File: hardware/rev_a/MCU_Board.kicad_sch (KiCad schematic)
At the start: 28 parts, among them J1 ST-Link, J2 Conn_01x08, J3 Bus, J4 Conn_01x08, J5 Conn_02x07_Odd_Even, SW1 nRST, U1 STM32F042K6Tx, U3 SN65HVD230, U4 LP2985-3.3, Y1 8Mhz

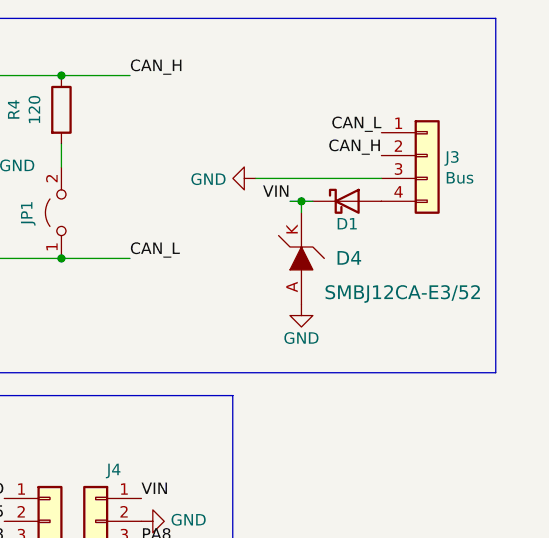
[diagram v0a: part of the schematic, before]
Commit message: Remove the dependancy with external libraries, the TVS diode is now using the default symbol and a custom footprint
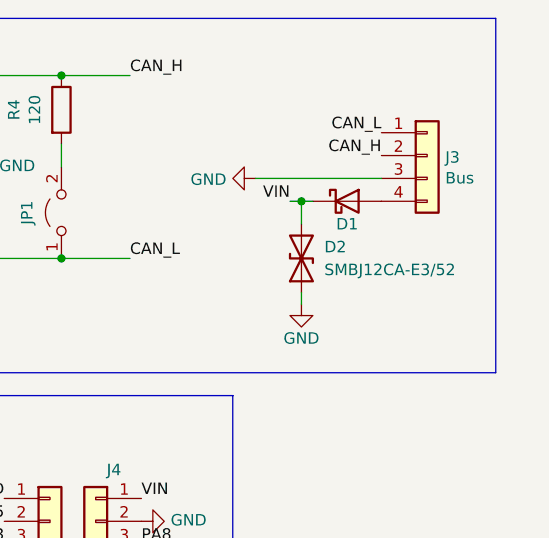
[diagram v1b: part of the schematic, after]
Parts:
- removed D4: SMBJ12CA-E3/52, custom:DO-214AA, symbol dk_TVS-Diodes:ESD5Z3_3T1G
- added D2: SMBJ12CA-E3/52, custom:DO-214AA, symbol Device:D_TVS
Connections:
- net GND: now also D2.1 (A1)
- net VIN: now also D2.2 (A2)
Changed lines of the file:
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@@
+    (stroke (width 0) (type default))
+  )
+  (wire (pts (xy 259.08 54.61) (xy 259.08 55.88))
     (stroke (width 0) (type default))
   )
@@
     (stroke (width 0) (type default))
   )
-  (wire (pts (xy 259.08 44.45) (xy 259.08 45.72))
+  (wire (pts (xy 259.08 44.45) (xy 259.08 46.99))
     (stroke (width 0) (type default))
   )
@@
     )
   )
-  (symbol (lib_id "dk_TVS-Diodes:ESD5Z3_3T1G") (at 259.08 50.8 90) (unit 1)
-    (in_bom yes) (on_board yes) (dnp no)
-    (property "Reference" "D4" (at 262.89 50.8 90)
-      (effects (font (size 1.524 1.524)) (justify right))
-    )
-    (property "Value" "SMBJ12CA-E3/52" (at 261.62 54.61 90)
-      (effects (font (size 1.524 1.524)) (justify right))
-    )
-    (property "Footprint" "custom:DO-214AA" (at 254 45.72 0)
-      (effects (font (size 1.524 1.524)) (justify left) hide)
-    )
-    (property "Datasheet" "https://fr.farnell.com/vishay/smbj12ca-e3-52/diode-tvs-600w-12v-bidir-smb/dp/1698866" (at 251.46 45.72 0)
-      (effects (font (size 1.524 1.524)) (justify left) hide)
-    )
-    (pin "A")
-    (pin "K")
-    (instances
-      (project "MCU_Board"
-        (path "/a4fcdb05-5e54-43b8-a791-cc363feb7f77"
-          (reference "D4") (unit 1)
-        )
-      )
+  (symbol (lib_id "Device:D_TVS") (at 259.08 50.8 90) (unit 1)
+    (in_bom yes) (on_board yes) (dnp no) (fields_autoplaced)
+    (property "Reference" "D2" (at 261.62 49.53 90)
+      (effects (font (size 1.27 1.27)) (justify right))
+    )
+    (property "Value" "SMBJ12CA-E3/52" (at 261.62 52.07 90)
+      (effects (font (size 1.27 1.27)) (justify right))
+    )
+    (property "Footprint" "custom:DO-214AA" (at 259.08 50.8 0)
+      (effects (font (size 1.27 1.27)) hide)
+    )
+    (property "Datasheet" "https://fr.farnell.com/vishay/smbj12ca-e3-52/diode-tvs-600w-12v-bidir-smb/dp/1698866" (at 259.08 50.8 0)
+      (effects (font (size 1.27 1.27)) hide)
+    )
+    (pin "1")
+    (pin "2")
+    (instances
+      (project "MCU_Board"
+        (path "/a4fcdb05-5e54-43b8-a791-cc363feb7f77"
+          (reference "D2") (unit 1)
+        )
+      )

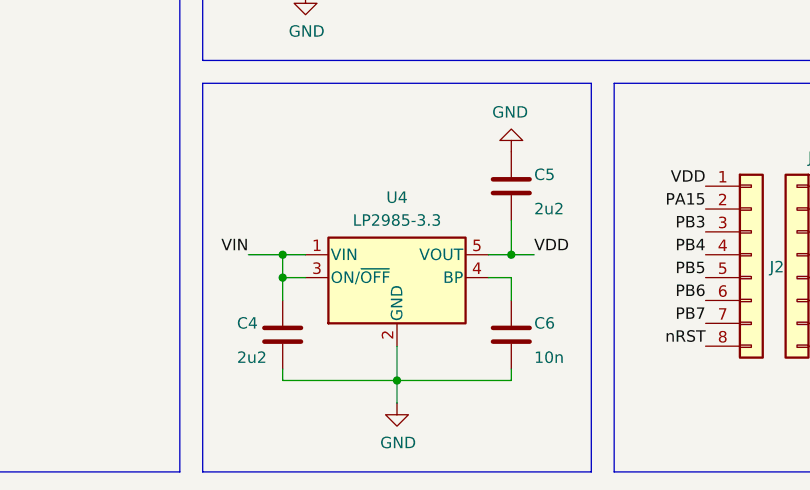
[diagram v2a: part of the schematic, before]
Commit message: Update the reference of various components
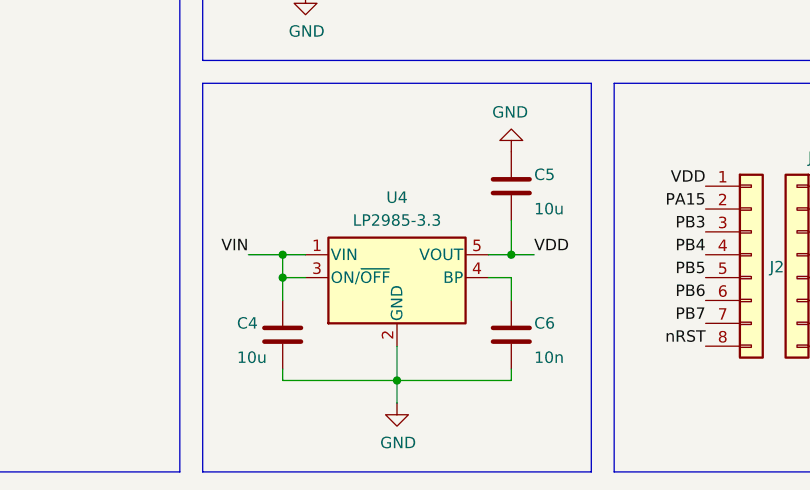
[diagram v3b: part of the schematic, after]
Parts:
- C4, C5: value 2u2 -> 10u
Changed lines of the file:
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@@
       (effects (font (size 1.27 1.27)) (justify left))
     )
-    (property "Value" "2u2" (at 173.99 96.52 0)
+    (property "Value" "10u" (at 173.99 96.52 0)
       (effects (font (size 1.27 1.27)) (justify left))
     )
@@
       (effects (font (size 1.27 1.27)) hide)
     )
-    (property "Datasheet" "https://fr.farnell.com/kemet/c0805c225k4pactu/condensateur-2-2-f-16v-10-x5r/dp/2773238" (at 179.07 93.98 0)
+    (property "Datasheet" "https://fr.farnell.com/walsin/0805x106m250cp/cap-10uf-25v-mlcc-0805/dp/3764157" (at 179.07 93.98 0)
       (effects (font (size 1.27 1.27)) hide)
     )
@@
       (effects (font (size 1.27 1.27)) hide)
     )
-    (property "Datasheet" "~" (at 133.35 74.93 0)
+    (property "Datasheet" "https://fr.farnell.com/amphenol-fci/10129381-914004blf/conn-header-14-voies-2-rangs-2/dp/3881595" (at 133.35 74.93 0)
       (effects (font (size 1.27 1.27)) hide)
     )
@@
       (effects (font (size 1.27 1.27)) (justify left))
     )
-    (property "Value" "2u2" (at 207.01 80.01 0)
+    (property "Value" "10u" (at 207.01 80.01 0)
       (effects (font (size 1.27 1.27)) (justify left))
     )
@@
       (effects (font (size 1.27 1.27)) hide)
     )
-    (property "Datasheet" "https://fr.farnell.com/kemet/c0805c225k4pactu/condensateur-2-2-f-16v-10-x5r/dp/2773238" (at 204.47 77.47 0)
-      (effects (font (size 1.27 1.27)) hide)
-    )
+    (property "Datasheet" "https://fr.farnell.com/walsin/0805x106m250cp/cap-10uf-25v-mlcc-0805/dp/3764157" (at 204.47 77.47 0)
+      (effects (font (size 1.27 1.27)) hide)
+    )

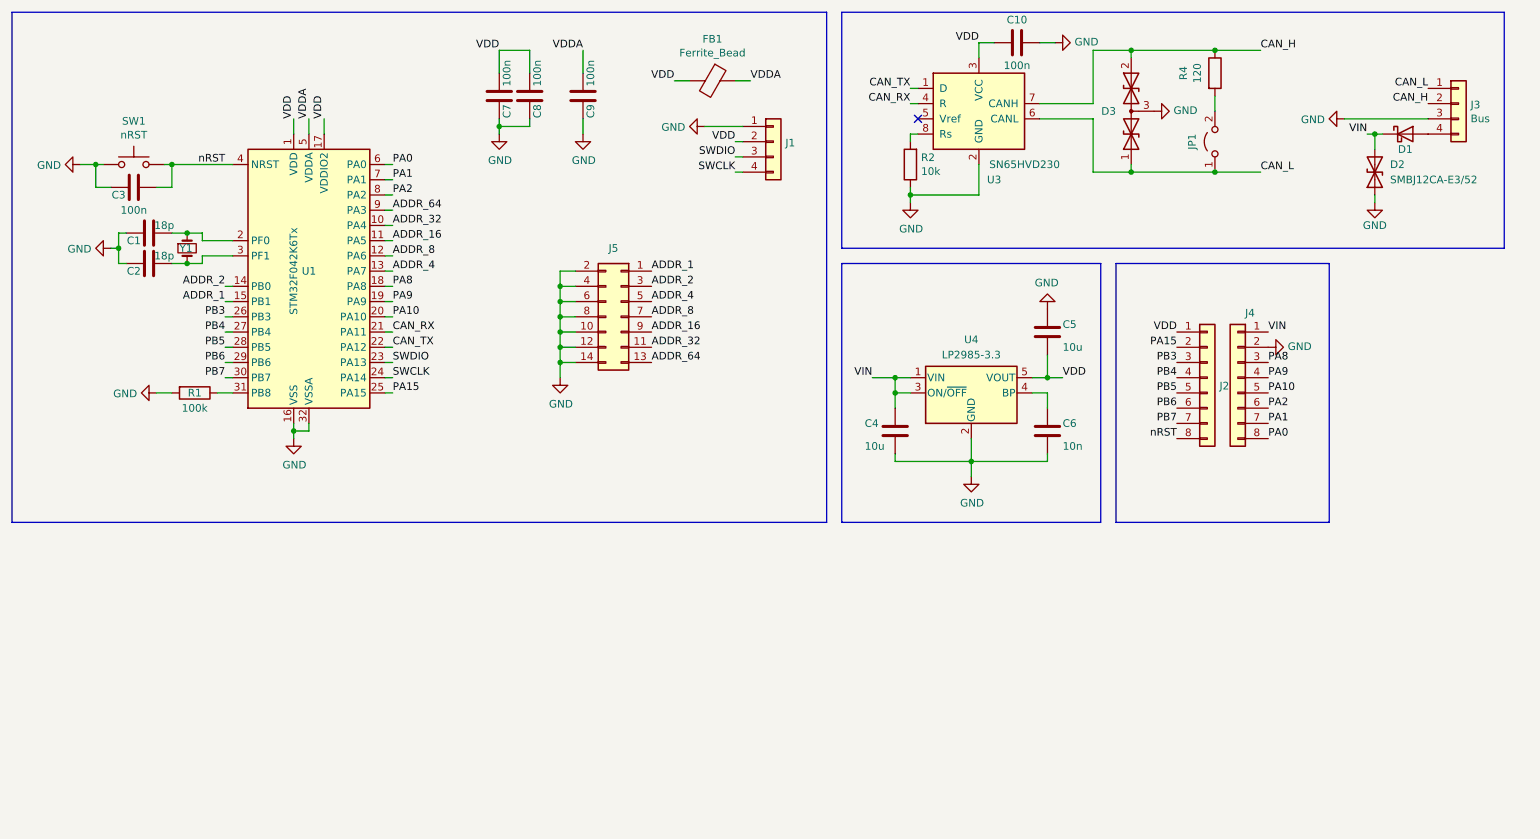
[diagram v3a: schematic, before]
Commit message: Refactorisation de l'étage d'entrée en utilisant un régulateur à découpage DC/DC type buck
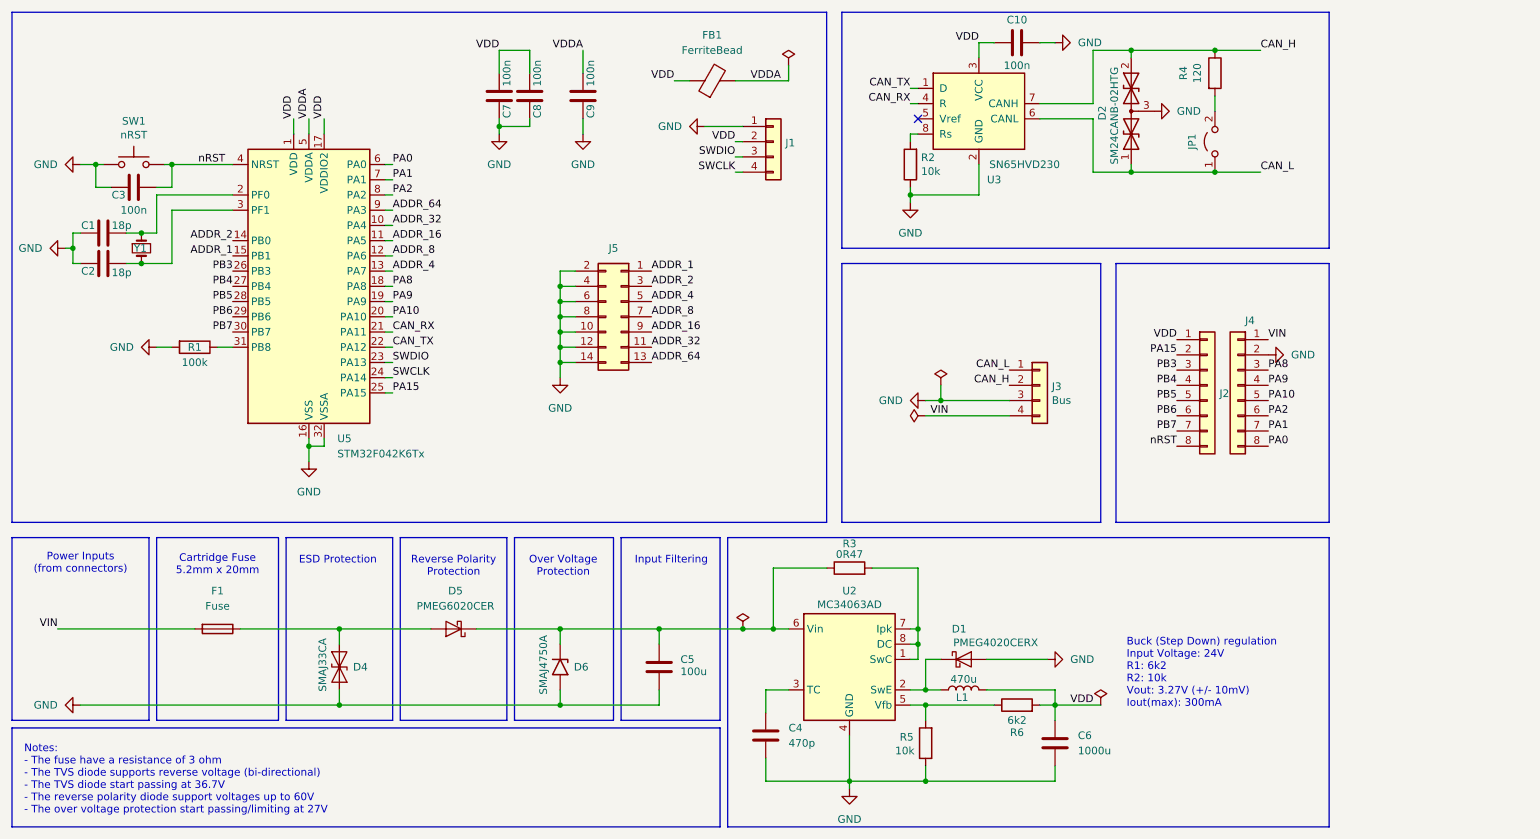
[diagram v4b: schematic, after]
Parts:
- removed D1: PMEG3020EJ,115, Diode_SMD:D_SOD-323F, symbol Device:D_Schottky
- removed D2: SMBJ12CA-E3/52, custom:DO-214AA, symbol Device:D_TVS
- removed D3: SM24CANB-02HTG, Package_TO_SOT_SMD:SOT-23_Handsoldering, symbol Device:D_TVS_Dual_AAC
- removed FB1: Ferrite_Bead, Inductor_SMD:L_0805_2012Metric_Pad1.15x1.40mm_HandSolder, symbol MCU_Board-rescue:Ferrite_Bead-Device
- removed U1: STM32F042K6Tx, Package_QFP:LQFP-32_7x7mm_P0.8mm, symbol MCU_Board-rescue:STM32F042K6Tx-MCU_ST_STM32F0
- removed U4: LP2985-3.3, Package_TO_SOT_SMD:SOT-23-5, symbol Regulator_Linear:LP2985-3.3
- added D1: PMEG4020CERX, Diode_SMD:Nexperia_CFP3_SOD-123W, symbol Diode:PMEG4020ER
- added D2: SM24CANB-02HTG, Package_TO_SOT_SMD:SOT-23_Handsoldering, symbol Device:D_TVS_Dual_AAC
- added D4: SMAJ33CA, Diode_SMD:D_SMA, symbol Diode:SMAJ33CA
- added D5: PMEG6020CER, Diode_SMD:Nexperia_CFP3_SOD-123W, symbol Diode:PMEG6020ER
- added D6: SMAJ4750A, Diode_SMD:D_SMA, symbol Diode:SMAJ45A
- added F1: Fuse, Fuse:Fuseholder_Clip-5x20mm_Littelfuse_100_Inline_P20.50x4.60mm_D1.30mm_Horizontal, symbol Device:Fuse
- added FB1: FerriteBead, Inductor_SMD:L_0805_2012Metric_Pad1.05x1.20mm_HandSolder, symbol Device:FerriteBead
- added L1: 470u, Inductor_THT:L_Radial_D8.7mm_P5.00mm_Fastron_07HCP, symbol Device:L
- added R3: 0R47, Resistor_SMD:R_0805_2012Metric_Pad1.20x1.40mm_HandSolder, symbol Device:R
- added R5: 10k, Resistor_SMD:R_0805_2012Metric_Pad1.20x1.40mm_HandSolder, symbol Device:R
- added R6: 6k2, Resistor_SMD:R_0805_2012Metric_Pad1.20x1.40mm_HandSolder, symbol Device:R
- added U2: MC34063AD, Package_SO:SOIC-8_3.9x4.9mm_P1.27mm, symbol Regulator_Switching:MC34063AD
- added U5: STM32F042K6Tx, Package_QFP:LQFP-32_7x7mm_P0.8mm, symbol MCU_ST_STM32F0:STM32F042K6Tx
- C4: value 10u -> 470p
- C5: value 10u -> 100u; footprint Capacitor_SMD:C_0805_2012Metric_Pad1.18x1.45mm_HandSolder -> Capacitor_THT:CP_Radial_D10.0mm_P5.00mm
- C6: value 10n -> 1000u; footprint Capacitor_SMD:C_0805_2012Metric_Pad1.18x1.45mm_HandSolder -> Capacitor_THT:CP_Radial_D10.0mm_P5.00mm
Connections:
- net ADDR_1: now also U5.15 (PB1)
- net ADDR_16: now also U5.11 (PA5)
- net ADDR_2: now also U5.14 (PB0)
- net ADDR_32: now also U5.10 (PA4)
- net ADDR_4: now also U5.13 (PA7)
- net ADDR_64: now also U5.9 (PA3)
- net ADDR_8: now also U5.12 (PA6)
- net CAN_H: now also D2.2 (A2)
- net CAN_L: now also D2.1 (A1)
- net CAN_RX: now also U5.21 (PA11)
- net CAN_TX: now also U5.22 (PA12)
- net GND: now also C5.2, D1.2 (A), D2.3 (common), D4.1 (A1), D6.2 (A2), R5.1, U2.4 (GND), U5.16 (VSS), U5.32 (VSSA); no longer C5.1
- net PA0: now also U5.6 (PA0)
- net PA1: now also U5.7 (PA1)
- net PA10: now also U5.20 (PA10)
- net PA15: now also U5.25 (PA15)
- net PA2: now also U5.8 (PA2)
- net PA8: now also U5.18 (PA8)
- net PA9: now also U5.19 (PA9)
- net PB3: now also U5.26 (PB3)
- net PB4: now also U5.27 (PB4)
- net PB5: now also U5.28 (PB5)
- net PB6: now also U5.29 (PB6)
- net PB7: now also U5.30 (PB7)
- net SWCLK: now also U5.24 (PA14)
- net SWDIO: now also U5.23 (PA13)
- net VDD: now also C6.1, FB1.1, L1.2, R6.2, U5.1 (VDD), U5.17 (VDDIO2); no longer C5.2
- net VDDA: now also FB1.2, U5.5 (VDDA)
- net VIN: now also J3.4 (Pin_4), F1.2; no longer C4.1
- net nRST: now also U5.4 (NRST)
- net at C1.1, Y1.1: now also U5.2 (PF0)
- net at C2.1, Y1.2: now also U5.3 (PF1)
- net at R1.1: now also U5.31 (PB8)
- new net: R5.2, R6.1, U2.5 (Vfb)
- new net: C5.1, D5.1 (K), D6.1 (A1), R3.1, U2.6 (Vin)
- new net: R3.2, U2.1 (SwC), U2.7 (Ipk), U2.8 (DC)
- new net: D1.1 (K), L1.1, U2.2 (SwE)
- new net: D4.2 (A2), D5.2 (A), F1.1
- new net: C4.1, U2.3 (TC)
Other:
- note added: "Buck (Step Down) regulation Input Voltage: 24V R1: 6k2 R2: 10k Vout: 3.27V (+/- 10mV) Iout(max): 300mA"
- note added: "Cartridge Fuse 5.2mm x 20mm"
- note added: "ESD Protection"
- note added: "Input Filtering"
- note added: "Notes: - The fuse have a resistance of 3 ohm - The TVS diode supports reverse voltage (bi-directional) - The TVS diode start passing at 36.7V - The reverse polarity diode support voltages up to 60V - The over voltage protection start passing/limiting at 27V"
- note added: "Over Voltage Protection"
- note added: "Power Inputs (from connectors)"
- note added: "Reverse Polarity Protection"
- moved on the sheet: C1, C2, J2, J3, J4, R1, Y1
